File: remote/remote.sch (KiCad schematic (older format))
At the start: 5 parts

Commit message: WIP switch to p-channel mosfet
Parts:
- removed Q?: 2N7002, Package_TO_SOT_SMD:SOT-23, symbol Transistor_FET:2N7002
- added Q?: AO3401A, Package_TO_SOT_SMD:SOT-23, symbol Transistor_FET:AO3401A
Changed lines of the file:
@@
 	5350 1350 5500 1350
 $Comp
-L Transistor_FET:2N7002 Q?
-U 1 1 5F7C47E5
-P 6400 1350
-F 0 "Q?" H 6604 1396 50  0000 L CNN
-F 1 "2N7002" H 6604 1305 50  0000 L CNN
-F 2 "Package_TO_SOT_SMD:SOT-23" H 6600 1275 50  0001 L CIN
-F 3 "https://www.fairchildsemi.com/datasheets/2N/2N7002.pdf" H 6400 1350 50  0001 L CNN
-	1    6400 1350
+L Transistor_FET:AO3401A Q?
+U 1 1 5F7D4874
+P 6550 1350
+F 0 "Q?" H 6755 1396 50  0000 L CNN
+F 1 "AO3401A" H 6755 1305 50  0000 L CNN
+F 2 "Package_TO_SOT_SMD:SOT-23" H 6750 1275 50  0001 L CIN
+F 3 "http://www.aosmd.com/pdfs/datasheet/AO3401A.pdf" H 6550 1350 50  0001 L CNN
+	1    6550 1350
 	1    0    0    -1
 $EndComp

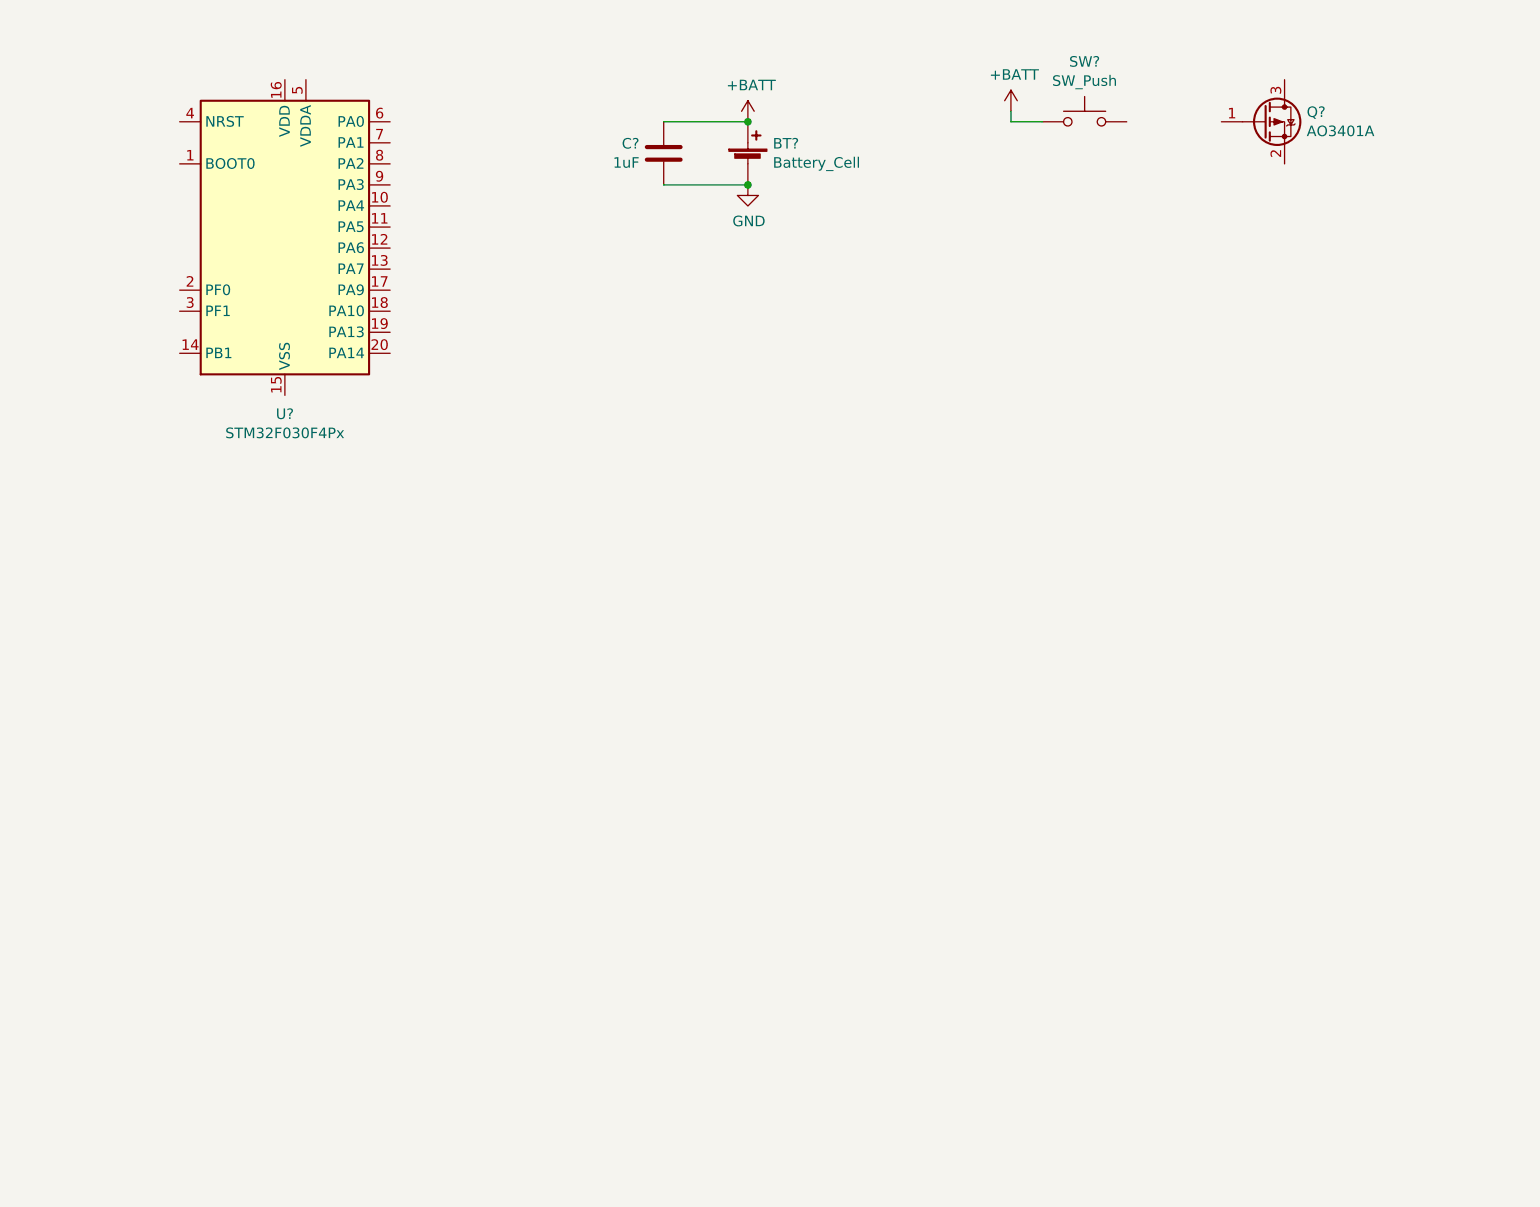
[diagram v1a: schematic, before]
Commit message: More schematic progress - add button circuits
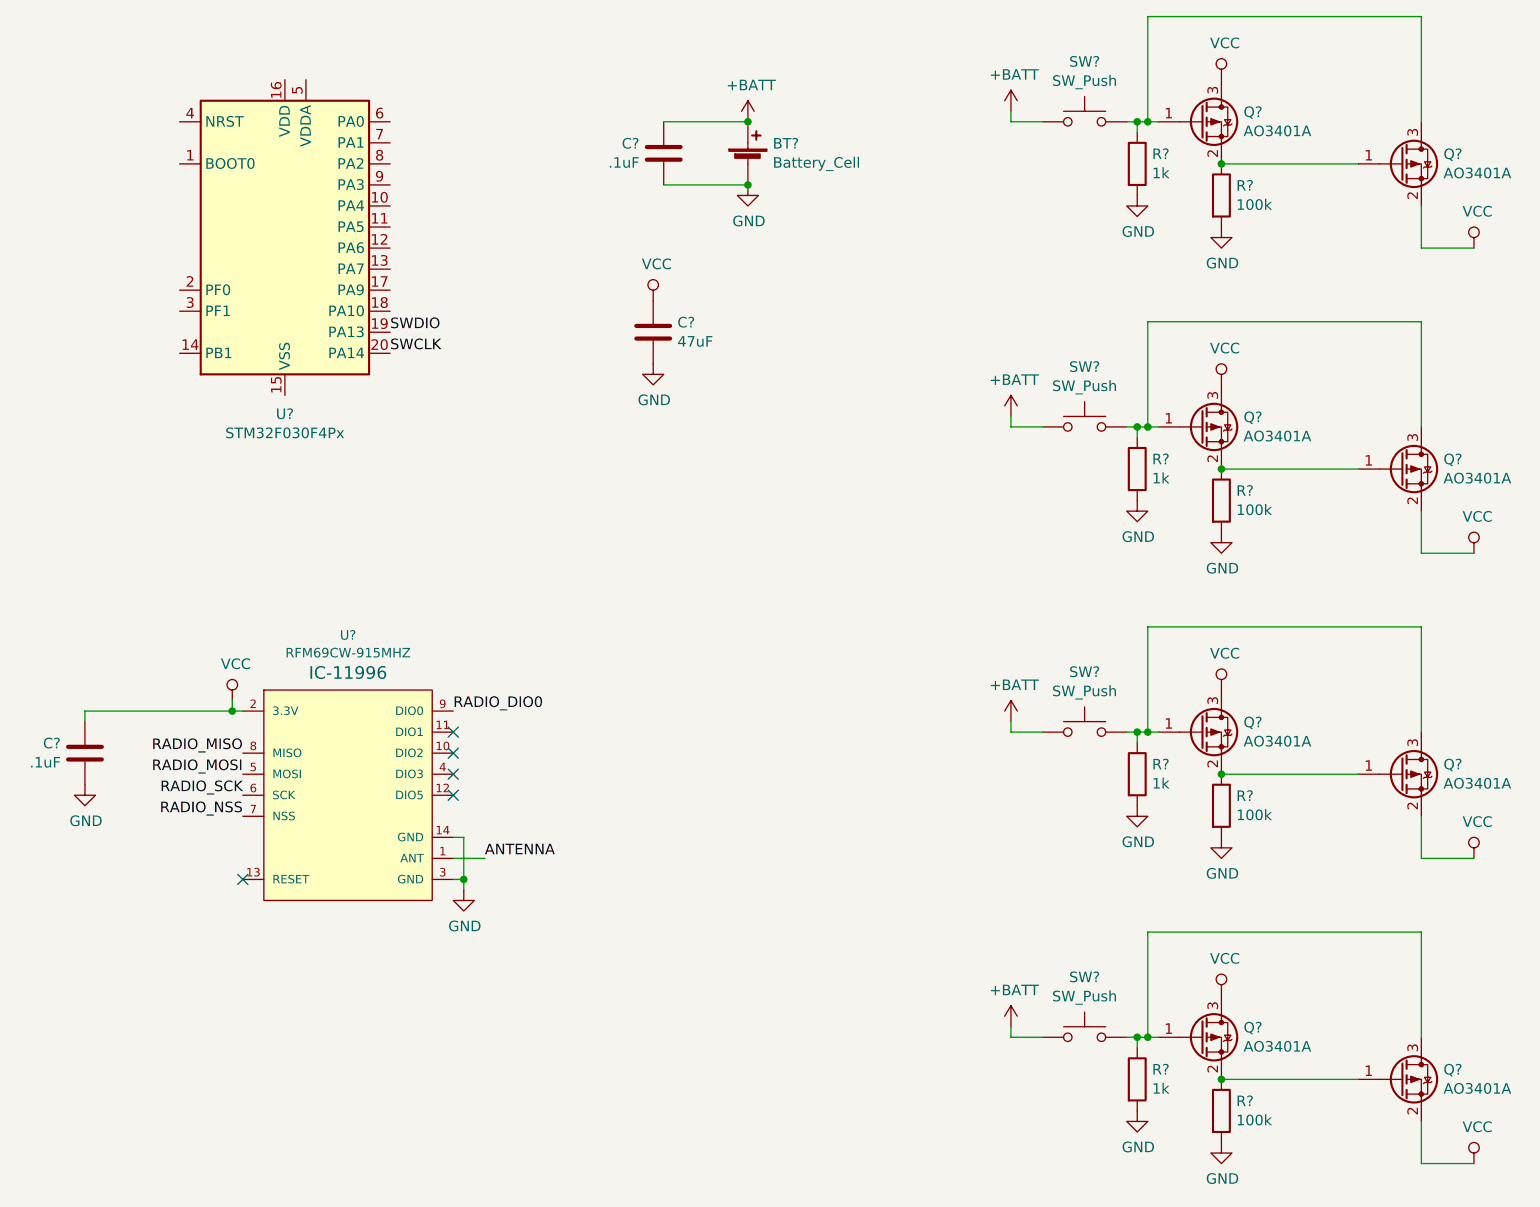
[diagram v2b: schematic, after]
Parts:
- added C?: 47uF, symbol Device:C
- added C?: .1uF, symbol Device:C
- added Q? (x7): AO3401A, Package_TO_SOT_SMD:SOT-23, symbol Transistor_FET:AO3401A
- added R? (x4): 100k, symbol Device:R
- added R? (x4): 1k, symbol Device:R
- added SW? (x3): SW_Push, symbol Switch:SW_Push
- added U?: RFM69CW-915MHZ, RFM69CW-XXXS2, symbol SparkFun-RF:RFM69CW-915MHZ
- C?: value 1uF -> .1uF
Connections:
- net +BATT: now also SW?.1, SW?.1, SW?.1
- net GND: now also C?.1, C?.2, R?.2, R?.2, R?.2, R?.2, R?.2, R?.2, R?.2, R?.2, U?.14 (GND), U?.3 (GND)
- net SWDIO: now reaches U?.19 (PA13)
- net SWCLK: now reaches U?.20 (PA14)
- net at SW?.2: now also Q?.1 (G), Q?.3 (D), R?.1
- net at Q?.2 (S): now also Q?.1 (G), R?.1
- net VCC: now reaches Q?.3 (D)
- net VCC: now also C?.1, C?.2, Q?.2 (S), Q?.2 (S), Q?.2 (S), Q?.2 (S), Q?.3 (D), Q?.3 (D), Q?.3 (D), U?.2 (3.3V)
- new net: Q?.1 (G), Q?.3 (D), R?.1, SW?.2 (x3)
- new net: Q?.1 (G), Q?.2 (S), R?.1 (x3)
- new net ANTENNA: U?.1 (ANT)
- new net RADIO_DIO0: U?.9 (DIO0)
- new net RADIO_MISO: U?.8 (MISO)
- new net RADIO_MOSI: U?.5 (MOSI)
- new net RADIO_NSS: U?.7 (NSS)
- new net RADIO_SCK: U?.6 (SCK)
- no-connect marks 0 -> 5
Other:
- moved on the sheet: Q?

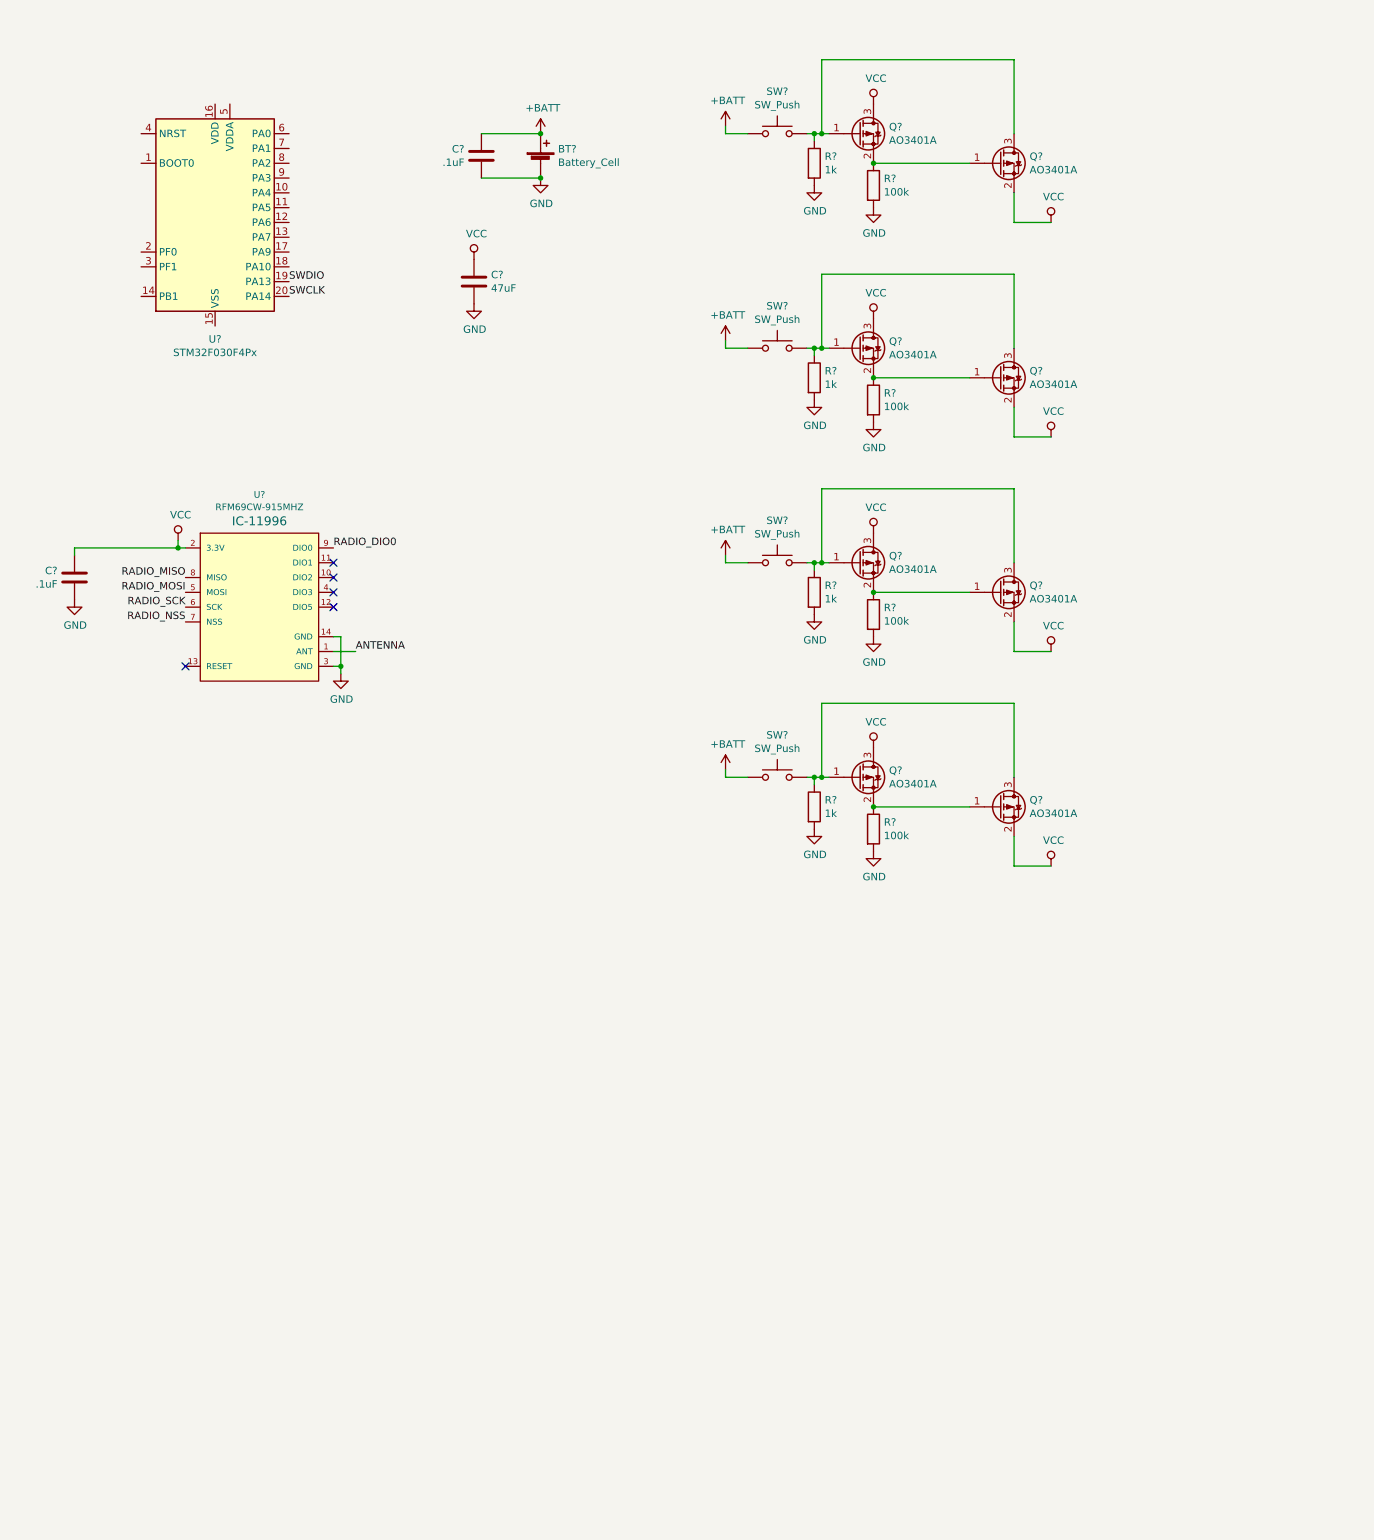
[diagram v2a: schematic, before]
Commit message: Fix button sensing
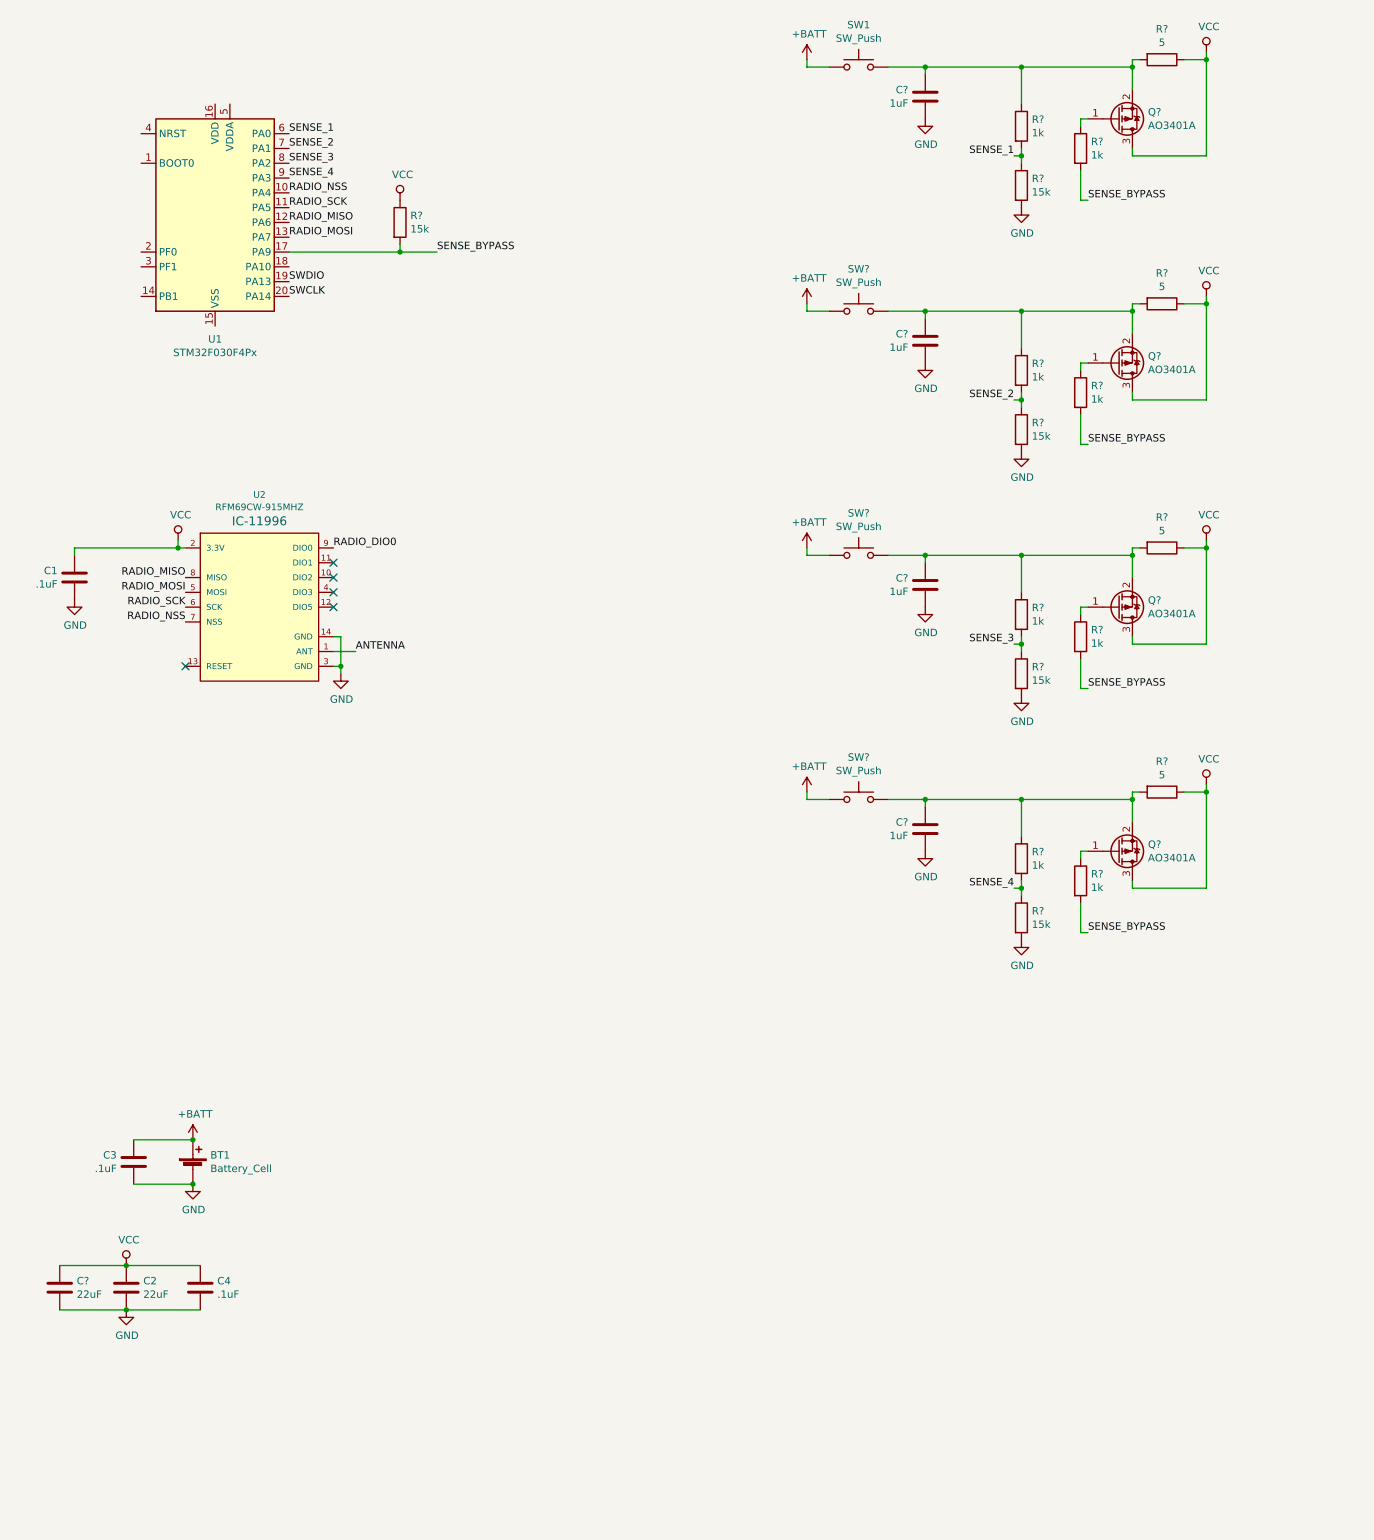
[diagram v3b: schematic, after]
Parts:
- removed Q? (x8): AO3401A, Package_TO_SOT_SMD:SOT-23, symbol Transistor_FET:AO3401A
- removed R? (x4): 100k, symbol Device:R
- removed R? (x4): 1k, symbol Device:R
- removed SW? (x3): SW_Push, symbol Switch:SW_Push
- added C4: .1uF, symbol Device:C
- added C? (x4): 1uF, symbol Device:C
- added C?: 22uF, symbol Device:C
- added Q? (x4): AO3401A, Package_TO_SOT_SMD:SOT-23, symbol Transistor_FET:AO3401A
- added R? (x4): 5, symbol Device:R
- added R? (x8): 1k, symbol Device:R
- added R? (x5): 15k, symbol Device:R
- added SW? (x3): SW_Push, symbol Switch:SW_Push
- C2: renamed from C?; value 47uF -> 22uF
- gave numbers to parts that had none: 6
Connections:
- net +BATT: now also SW?.1, SW?.1, SW?.1
- net GND: now also C4.1, C?.1, C?.1, C?.1, C?.1, C?.2, R?.2, R?.2, R?.2, R?.2
- net RADIO_MISO: now also U1.12 (PA6)
- net RADIO_MOSI: now also U1.13 (PA7)
- net RADIO_NSS: now also U1.10 (PA4)
- net RADIO_SCK: now also U1.11 (PA5)
- net VCC: now also C4.2, C?.1, Q?.3 (D), Q?.3 (D), Q?.3 (D), Q?.3 (D), R?.1, R?.1, R?.1, R?.1, R?.1
- net SENSE_BYPASS: now reaches U1.17 (PA9)
- net SENSE_BYPASS: now also R?.2, R?.2, R?.2, R?.2, R?.2
- net SENSE_1: now reaches U1.6 (PA0)
- net SENSE_1: now also R?.1, R?.2
- net SENSE_2: now reaches U1.7 (PA1)
- net SENSE_2: now also R?.1, R?.2
- net SENSE_3: now reaches U1.8 (PA2)
- net SENSE_3: now also R?.1, R?.2
- net SENSE_4: now reaches U1.9 (PA3)
- net SENSE_4: now also R?.1, R?.2
- net at SW1.2: now also C?.2, Q?.2 (S), R?.1, R?.2
- new net: Q?.1 (G), R?.1 (x4)
- new net: C?.2, Q?.2 (S), R?.1, R?.2, SW?.2 (x3)
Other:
- moved on the sheet: BT1, C2, C3, SW1
